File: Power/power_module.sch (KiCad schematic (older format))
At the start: 57 parts, among them J1 Conn_02x03_Odd_Even, J10 Conn_01x04, J11 Conn_02x02_Odd_Even, J2 Conn_02x03_Odd_Even, J3 Conn_02x06_Counter_Clockwise, J4 Conn_02x05_Top_Bottom, J5 Conn_02x05_Top_Bottom, J6 Conn_02x02_Odd_Even, J7 Conn_02x02_Odd_Even, J8 Conn_01x06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

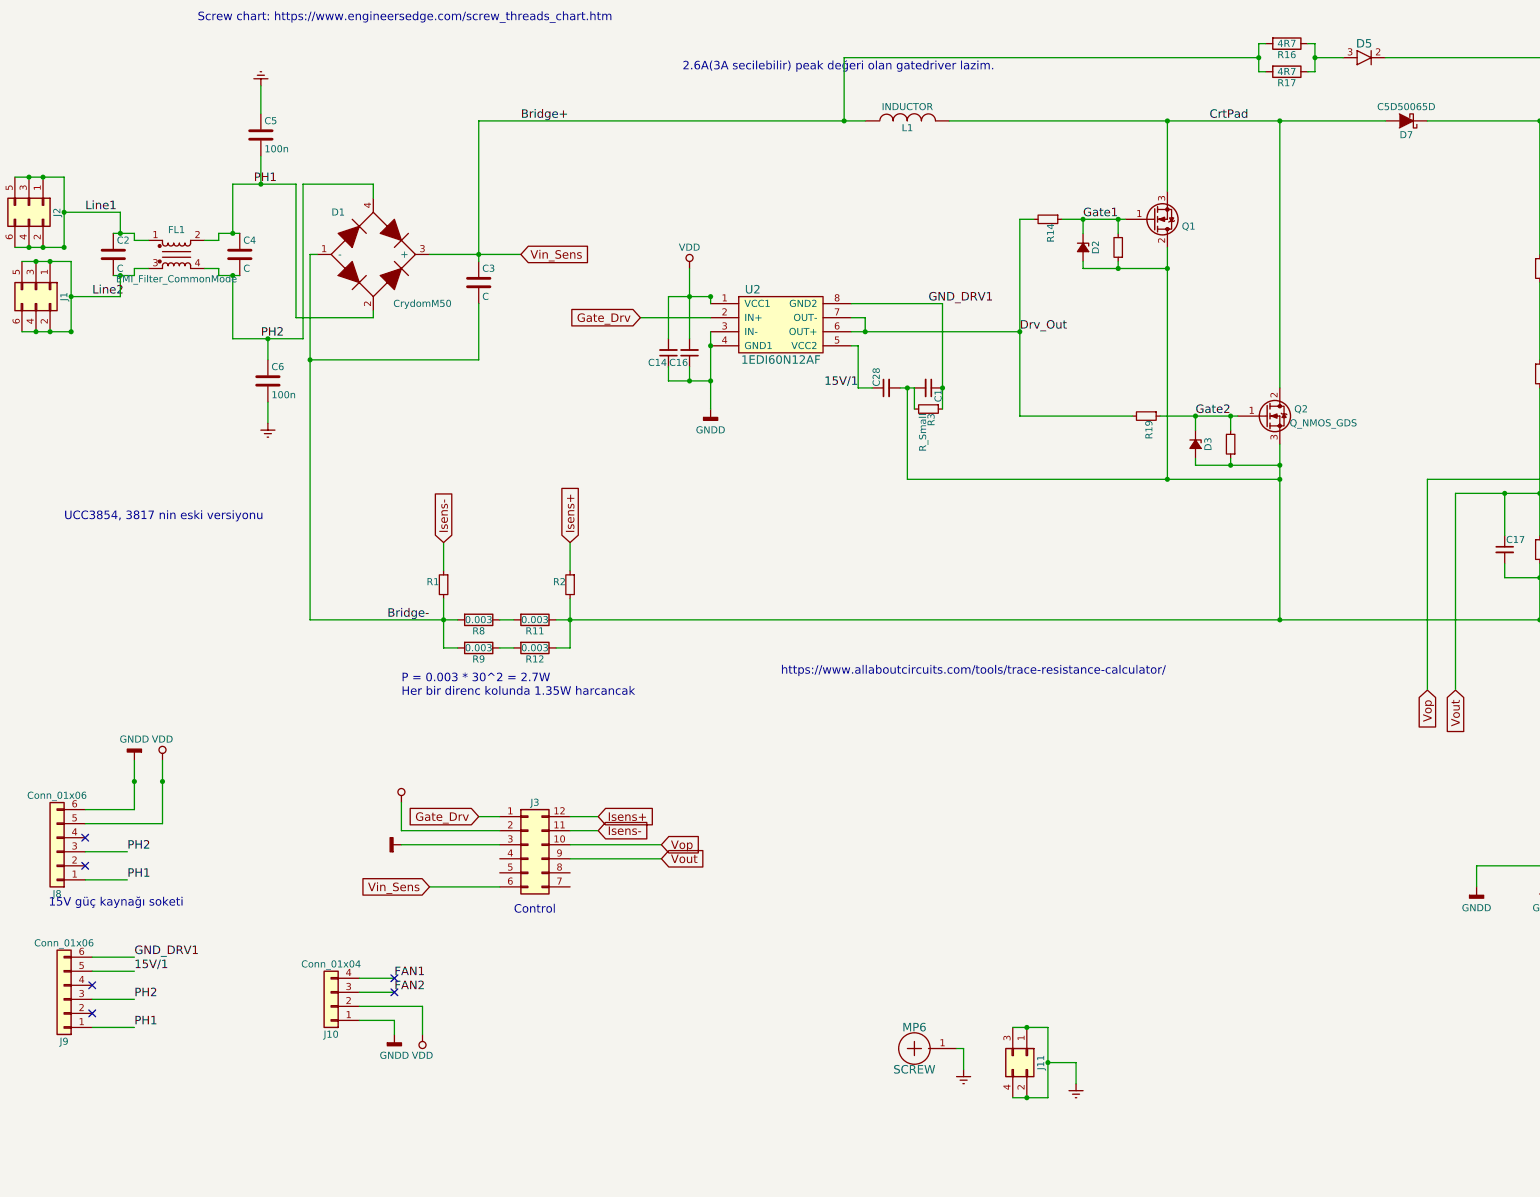
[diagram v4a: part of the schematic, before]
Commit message: Hatali Mosfet paketi duzeltildi. EMI filtre kaldirildi ve kart boyu kisaldi. TO247-2 paketli boost diyodu kullanildi.
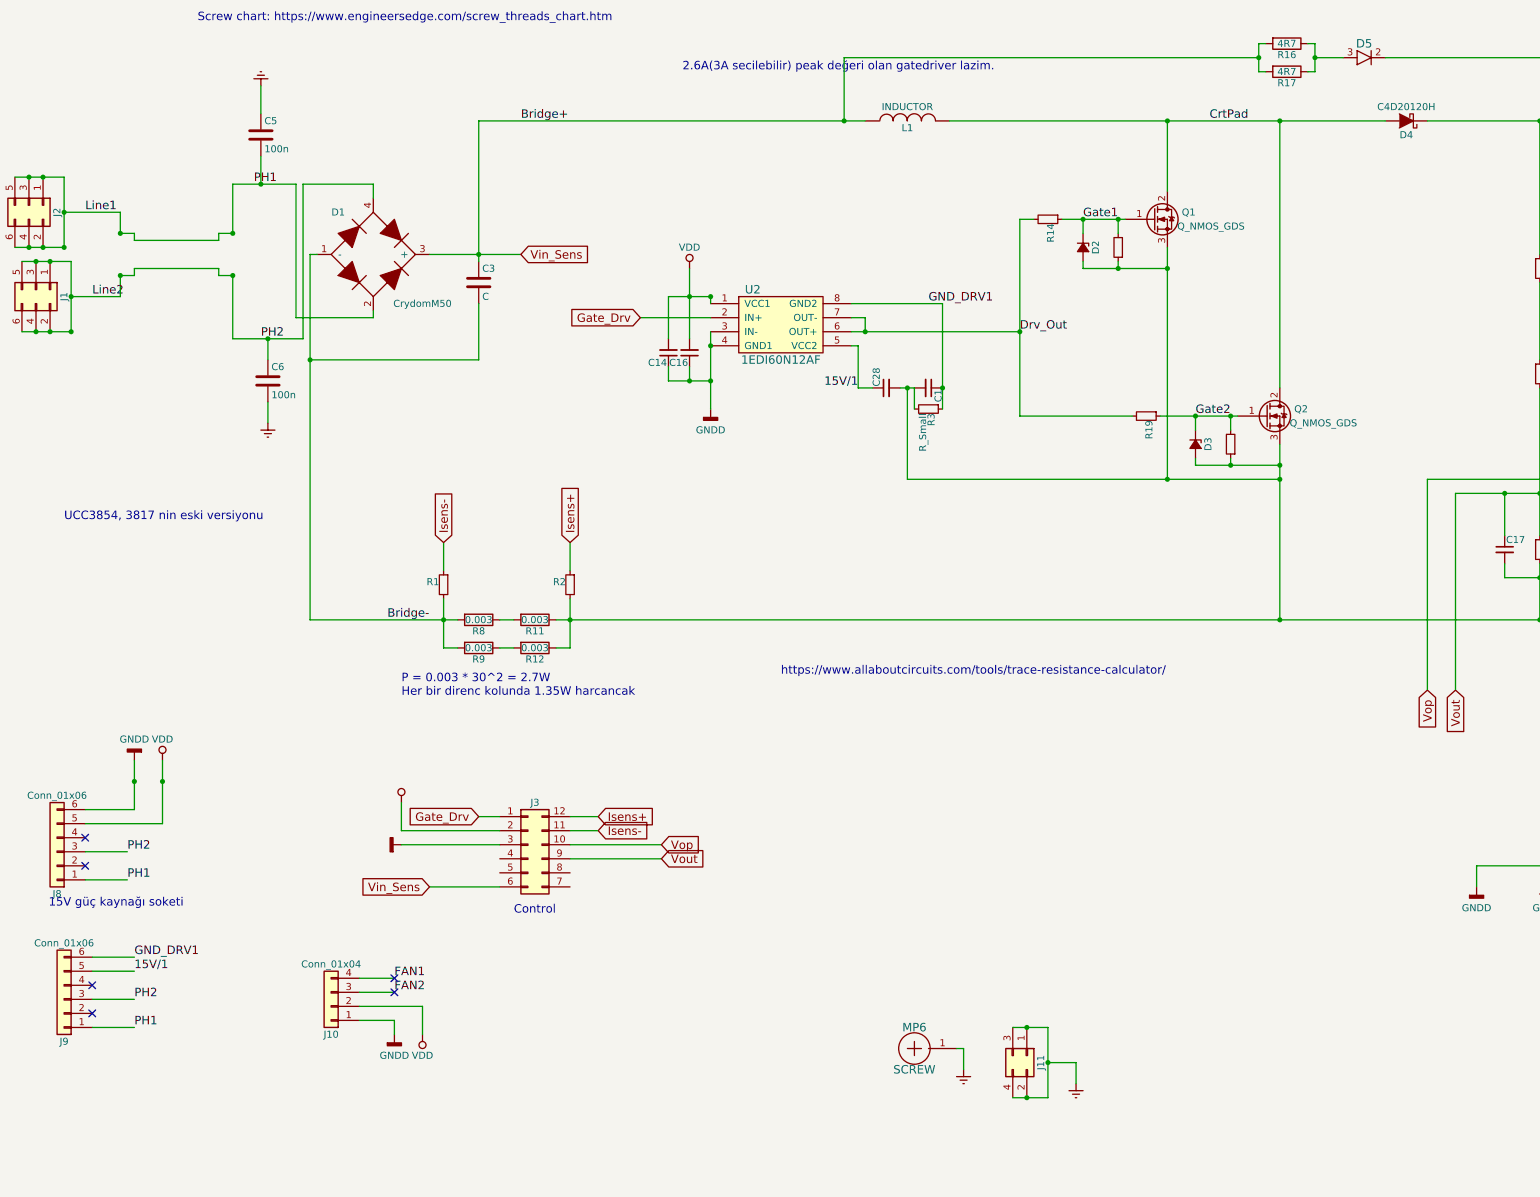
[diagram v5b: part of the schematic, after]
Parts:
- removed C2, C4: C, Capacitors_ThroughHole:CP_Axial_L30.0mm_D10.0mm_P35.00mm_Horizontal, symbol C
- removed D7: C5D50065D, TO_SOT_Packages_THT:TO-247_TO-3P_Vertical, symbol C5D50065D
- removed FL1: EMI_Filter_CommonMode, NamchoLibs:RB6522_Size4, symbol EMI_Filter_CommonMode
- added D4: C4D20120H, TO_SOT_Packages_THT:TO-247-2_Vertical, symbol C4D20120H
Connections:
- net PH1 is gone; now on net Line1: C5.2, D1.2, J8.1 (Pin_1), J9.1 (Pin_1)
- net PH2 is gone; now on net Line2: C6.1, D1.4, J8.3 (Pin_3), J9.3 (Pin_3)
- net CrtPad: now also Q1.2 (D), D4.2 (A); no longer Q1.3 (S)
- net GNDA: now also Q1.3 (S); no longer Q1.2 (D)
- net Vout+: now also D4.1 (K)
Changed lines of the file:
@@
-$EndComp
-$Comp
-L C5D50065D D7
-U 1 1 5AA8DE90
-P 10500 2000
-F 0 "D7" H 10500 2100 50  0000 C CNN
-F 1 "C5D50065D" H 10500 1900 50  0000 C CNN
-F 2 "TO_SOT_Packages_THT:TO-247_TO-3P_Vertical" H 10600 1800 50  0001 C CNN
-F 3 "" H 10500 2000 50  0000 C CNN
-	1    10500 2000
-	-1   0    0    1
 $EndComp
 $Comp
@@
 Text Label 6600 3900 2    60   ~ 0
 15V/1
-$Comp
-L Q_NMOS_GDS Q1
-U 1 1 5A5E6F51
-P 8700 2700
-F 0 "Q1" H 9000 2750 50  0000 R CNN
-F 1 "Q_NMOS_GDS" H 9350 2650 50  0001 R CNN
-F 2 "TO_SOT_Packages_THT:TO-247_TO-3P_Vertical" H 8900 2800 50  0001 C CNN
-F 3 "" H 8700 2700 50  0000 C CNN
-	1    8700 2700
-	1    0    0    1
-$EndComp
 $Comp
 L R R16
@@
 	0    1    1    0
 $EndComp
-$Comp
-L EMI_Filter_CommonMode FL1
-U 1 1 5B1CED70
-P 1750 2950
-F 0 "FL1" H 1750 3125 50  0000 C CNN
-F 1 "EMI_Filter_CommonMode" H 1750 2775 50  0000 C CNN
-F 2 "NamchoLibs:RB6522_Size4" V 1750 2990 50  0001 C CNN
-F 3 "" V 1750 2990 50  0000 C CNN
-	1    1750 2950
-	1    0    0    -1
-$EndComp
-$Comp
-L C C2
-U 1 1 5B1CF825
-P 1300 2950
-F 0 "C2" H 1325 3050 50  0000 L CNN
-F 1 "C" H 1325 2850 50  0000 L CNN
-F 2 "Capacitors_ThroughHole:CP_Axial_L30.0mm_D10.0mm_P35.00mm_Horizontal" H 1338 2800 50  0001 C CNN
-F 3 "" H 1300 2950 50  0001 C CNN
-	1    1300 2950
-	1    0    0    -1
-$EndComp
-$Comp
-L C C4
-U 1 1 5B1CFA6B
-P 2200 2950
-F 0 "C4" H 2225 3050 50  0000 L CNN
-F 1 "C" H 2225 2850 50  0000 L CNN
-F 2 "Capacitors_ThroughHole:CP_Axial_L30.0mm_D10.0mm_P35.00mm_Horizontal" H 2238 2800 50  0001 C CNN
-F 3 "" H 2200 2950 50  0001 C CNN
-	1    2200 2950
-	1    0    0    -1
-$EndComp
 Connection ~ 4550 5550
 Connection ~ 3650 5550
@@
 Connection ~ 6950 3900
 Wire Wire Line
-	1300 2800 1450 2800
+	1350 2800 1450 2800
 Wire Wire Line
 	1450 2800 1450 2850
 Wire Wire Line
-	1450 2850 1550 2850
-Wire Wire Line
-	1550 3050 1450 3050
+	1450 2850 2050 2850
+Wire Wire Line
+	1450 3050 2050 3050
 Wire Wire Line
 	1450 3050 1450 3100
 Wire Wire Line
-	1450 3100 1300 3100
-Wire Wire Line
-	1950 2850 2050 2850
+	1450 3100 1350 3100
 Wire Wire Line
 	2050 2850 2050 2800
 Wire Wire Line
-	2050 2800 2200 2800
-Wire Wire Line
-	1950 3050 2050 3050
+	2050 2800 2150 2800
 Wire Wire Line
 	2050 3050 2050 3100
 Wire Wire Line
-	2050 3100 2200 3100
+	2050 3100 2150 3100
 Wire Wire Line
 	950  2900 600  2900
@@
 Connection ~ 2150 3100
 Wire Wire Line
-	2150 2450 2150 2800
+	2150 2800 2150 2450
 Connection ~ 2150 2800
 Wire Wire Line
@@
 	7700 8450 7950 8450
 Wire Wire Line
-	7700 8950 7950 8950
-Wire Wire Line
-	7950 8950 7950 8450
+	7950 8950 7700 8950
+Wire Wire Line
+	7950 8450 7950 8950
 Connection ~ 7800 8950
 Connection ~ 7800 8450
@@
 Wire Wire Line
 	2400 4000 2400 4150
+$Comp
+L Q_NMOS_GDS Q1
+U 1 1 5B3035DE
+P 8700 2700
+F 0 "Q1" H 9000 2750 50  0000 R CNN
+F 1 "Q_NMOS_GDS" H 9350 2650 50  0000 R CNN
+F 2 "TO_SOT_Packages_THT:TO-247_TO-3P_Vertical" H 8900 2800 50  0001 C CNN
+F 3 "" H 8700 2700 50  0000 C CNN
+	1    8700 2700
+	1    0    0    -1
+$EndComp
+$Comp
+L C4D20120H D4
+U 1 1 5B31658D
+P 10500 2000
+F 0 "D4" H 10500 2100 50  0000 C CNN
+F 1 "C4D20120H" H 10500 1900 50  0000 C CNN
+F 2 "TO_SOT_Packages_THT:TO-247-2_Vertical" H 10600 1800 50  0001 C CNN
+F 3 "" H 10500 2000 50  0000 C CNN
+	1    10500 2000
+	-1   0    0    1
+$EndComp
 $EndSCHEMATC
